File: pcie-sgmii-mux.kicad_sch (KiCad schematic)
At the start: 16 parts, among them U15 TMUXHS4412RUAR

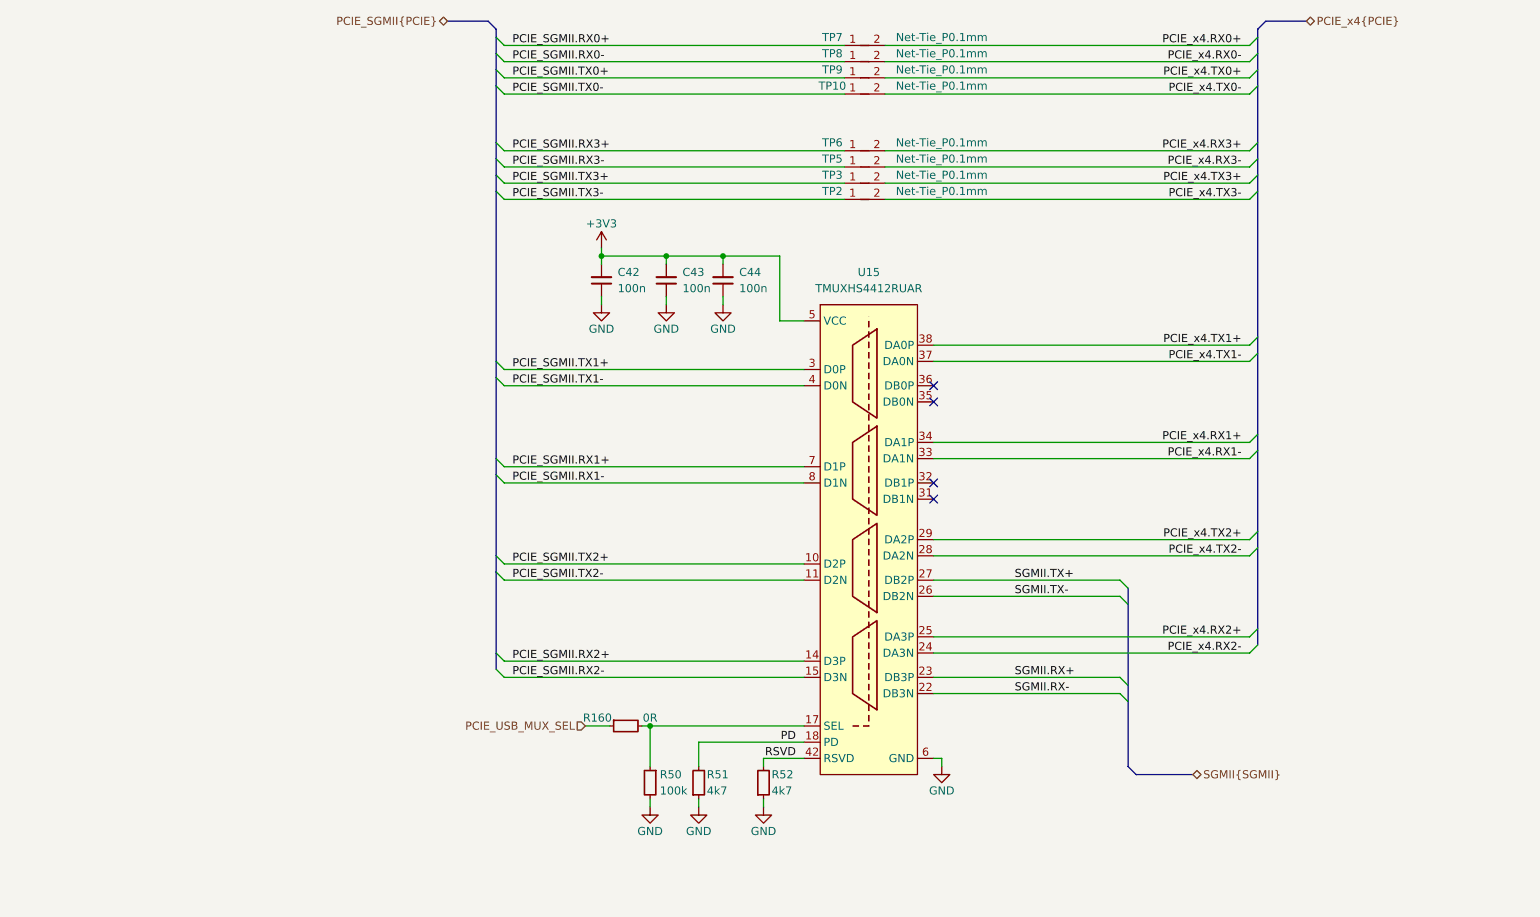
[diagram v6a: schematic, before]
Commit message: [#83338] Fixed PCIe TX/RX
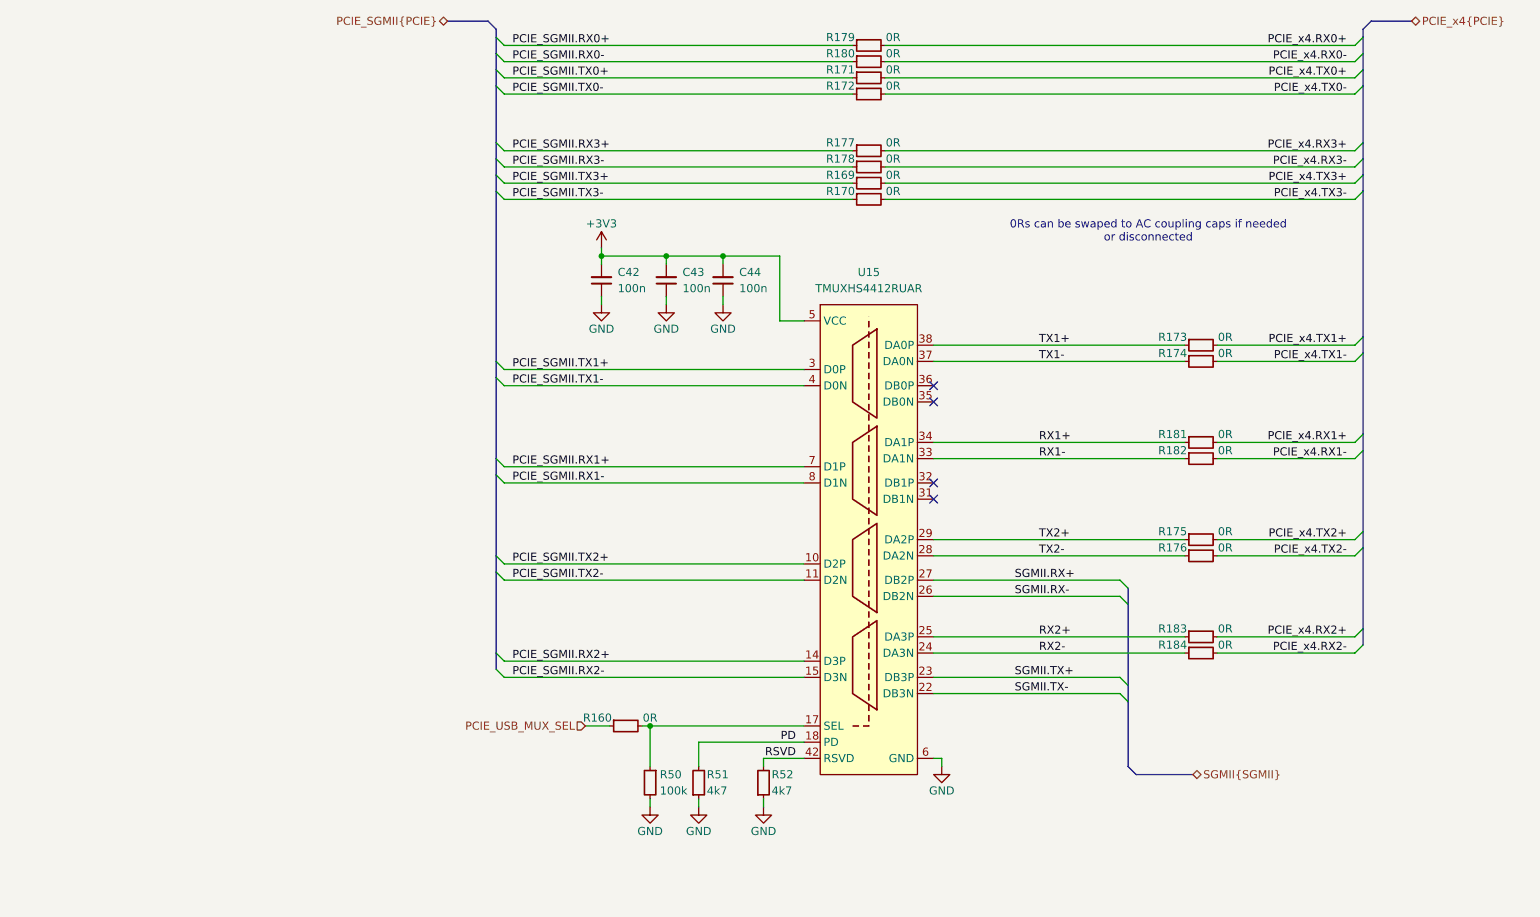
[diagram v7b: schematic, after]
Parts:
- removed TP10, TP2, TP3, TP5, TP6, TP7, TP8, TP9: Net-Tie_P0.1mm, antmicro-footprints:NetTie-2_SMD_Pad0.1mm, symbol antmicroShuntsJumpers:Net-Tie_P0.1mm
- added R169, R170, R171, R172, R173, R174, R175, R176, R177, R178, R179, R180, R181, R182, R183, R184: R_0R_0402, antmicro-footprints:R_0402_1005Metric, symbol antmicroResistors0402:R_0R_0402
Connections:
- net PCIE_SGMII.RX0+: now also R179.1
- net PCIE_SGMII.RX0-: now also R180.1
- net PCIE_SGMII.RX3+: now also R177.1
- net PCIE_SGMII.RX3-: now also R178.1
- net PCIE_SGMII.TX0+: now also R171.1
- net PCIE_SGMII.TX0-: now also R172.1
- net PCIE_SGMII.TX3+: now also R169.1
- net PCIE_SGMII.TX3-: now also R170.1
- net PCIE_x4.RX0+: now also R179.2
- net PCIE_x4.RX0-: now also R180.2
- net PCIE_x4.RX1+: now also R181.2; no longer U15.34 (DA1P)
- net PCIE_x4.RX1-: now also R182.2; no longer U15.33 (DA1N)
- net PCIE_x4.RX2+: now also R183.2; no longer U15.25 (DA3P)
- net PCIE_x4.RX2-: now also R184.2; no longer U15.24 (DA3N)
- net PCIE_x4.RX3+: now also R177.2
- net PCIE_x4.RX3-: now also R178.2
- net PCIE_x4.TX0+: now also R171.2
- net PCIE_x4.TX0-: now also R172.2
- net PCIE_x4.TX1+: now also R173.2; no longer U15.38 (DA0P)
- net PCIE_x4.TX1-: now also R174.2; no longer U15.37 (DA0N)
- net PCIE_x4.TX2+: now also R175.2; no longer U15.29 (DA2P)
- net PCIE_x4.TX2-: now also R176.2; no longer U15.28 (DA2N)
- net PCIE_x4.TX3+: now also R169.2
- net PCIE_x4.TX3-: now also R170.2
- net SGMII.RX+: now also U15.27 (DB2P); no longer U15.23 (DB3P)
- net SGMII.RX-: now also U15.26 (DB2N); no longer U15.22 (DB3N)
- net SGMII.TX+: now also U15.23 (DB3P); no longer U15.27 (DB2P)
- net SGMII.TX-: now also U15.22 (DB3N); no longer U15.26 (DB2N)
- new net RX1+: R181.1, U15.34 (DA1P)
- new net RX1-: R182.1, U15.33 (DA1N)
- new net RX2+: R183.1, U15.25 (DA3P)
- new net RX2-: R184.1, U15.24 (DA3N)
- new net TX1+: R173.1, U15.38 (DA0P)
- new net TX1-: R174.1, U15.37 (DA0N)
- new net TX2+: R175.1, U15.29 (DA2P)
- new net TX2-: R176.1, U15.28 (DA2N)
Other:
- note added: "0Rs can be swaped to AC coupling caps if needed or disconnected"

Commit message: [#83609] Reannotate board
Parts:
- renumbered C42 to C125, C43 to C126, C44 to C127, R160 to R218, R50 to R219, R51 to R220, R52 to R221, R179 to R222, R180 to R223, R171 to R224, R172 to R225, R177 to R226, R178 to R227, R169 to R228, R170 to R229, R173 to R230, R174 to R231, R181 to R232, R182 to R233, R175 to R234, R176 to R235, R183 to R236, R184 to R237, U15 to U26
